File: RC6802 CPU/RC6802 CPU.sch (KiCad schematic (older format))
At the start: 53 parts, among them J1 RC6802_Backplane, J2 RC6802_UI_Port, J3 BARREL_JACK, J4 DECODED, M1 Mounting, M2 Mounting, M3 Mounting, M4 Mounting, U1 MC6802, U2 HM62256BLP-7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

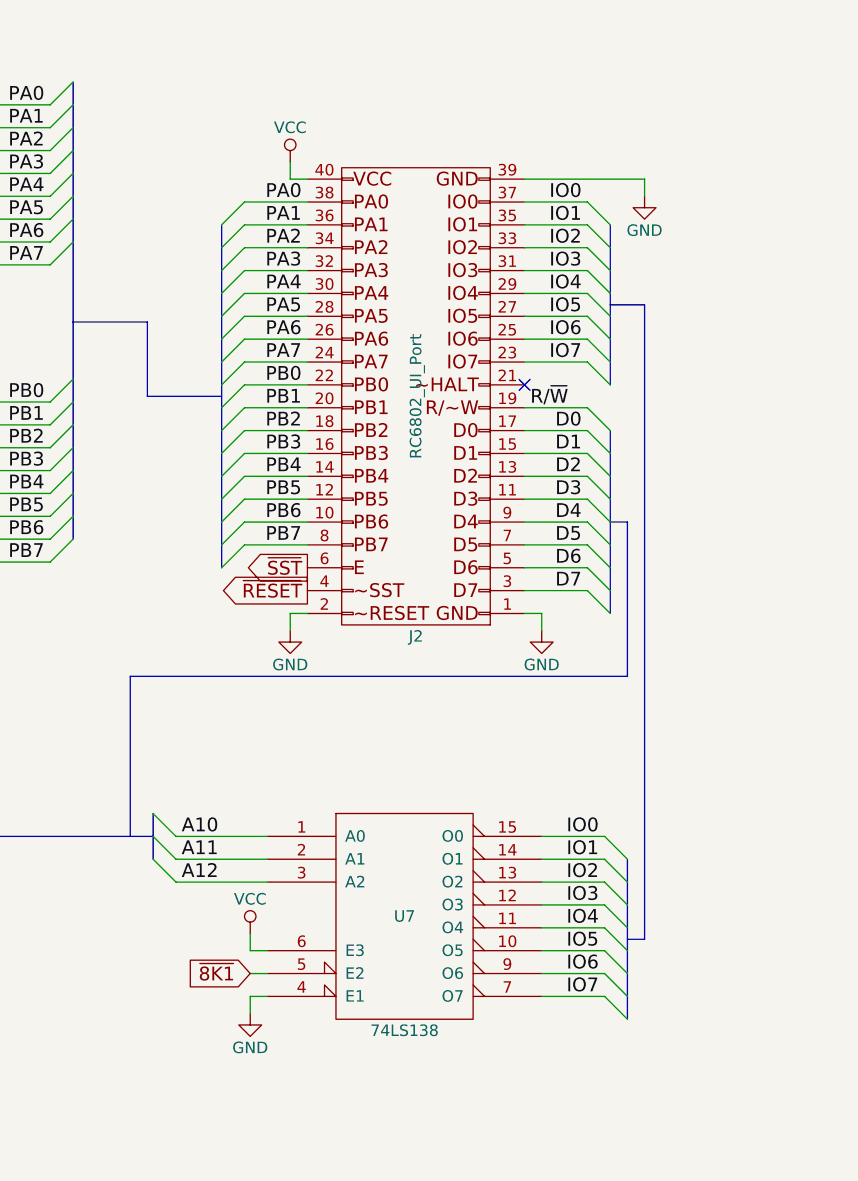
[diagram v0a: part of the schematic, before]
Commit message: UI board layout done
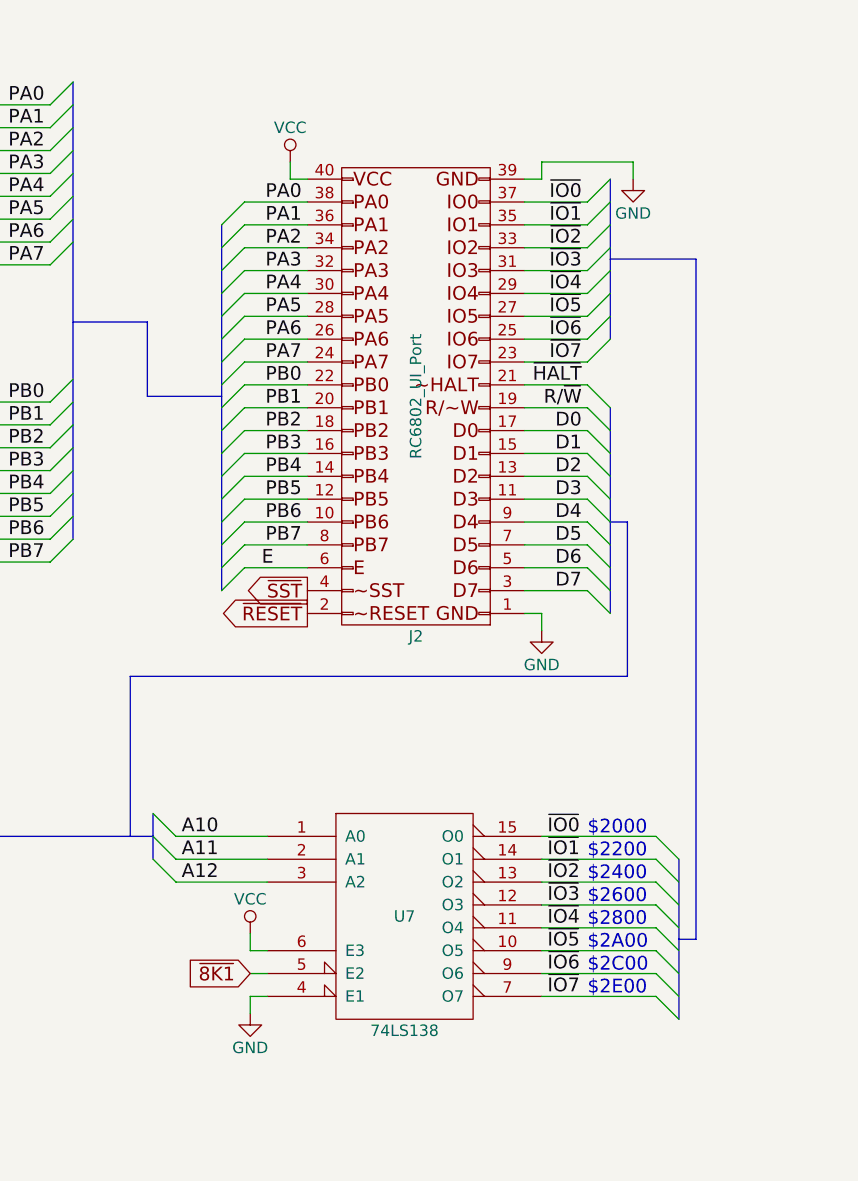
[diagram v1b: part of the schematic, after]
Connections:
- net E: now also J2.6 (P6)
- net GND: no longer J2.2 (P2)
- net ~HALT: now also J2.21 (P21)
- net ~RESET: now also J2.2 (P2); no longer J2.4 (P4)
- net ~SST: now also J2.4 (P4); no longer J2.6 (P6)
- net IO0 renamed ~IO0
- net IO1 renamed ~IO1
- net IO2 renamed ~IO2
- net IO3 renamed ~IO3
- net IO4 renamed ~IO4
- net IO5 renamed ~IO5
- net IO6 renamed ~IO6
- net IO7 renamed ~IO7
- no-connect marks 17 -> 16
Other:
- note added: "$2200"
- note added: "$2400"
- note added: "$2600"
- note added: "$2800"
- note added: "$2A00"
- note added: "$2C00"
- note added: "$2E00"
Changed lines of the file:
@@
 L GND #PWR05
 U 1 1 5D65DEF6
-P 10725 2425
-F 0 "#PWR05" H 10725 2175 50  0001 C CNN
-F 1 "GND" H 10725 2275 50  0000 C CNN
-F 2 "" H 10725 2425 50  0001 C CNN
-F 3 "" H 10725 2425 50  0001 C CNN
-	1    10725 2425
+P 10675 2350
+F 0 "#PWR05" H 10675 2100 50  0001 C CNN
+F 1 "GND" H 10675 2200 50  0000 C CNN
+F 2 "" H 10675 2350 50  0001 C CNN
+F 3 "" H 10675 2350 50  0001 C CNN
+	1    10675 2350
 	1    0    0    -1
 $EndComp
@@
 $EndComp
 $Comp
-L GND #PWR010
-U 1 1 5D729D92
-P 9175 4325
-F 0 "#PWR010" H 9175 4075 50  0001 C CNN
-F 1 "GND" H 9175 4175 50  0000 C CNN
-F 2 "" H 9175 4325 50  0001 C CNN
-F 3 "" H 9175 4325 50  0001 C CNN
-	1    9175 4325
-	1    0    0    -1
-$EndComp
-$Comp
 L GND #PWR011
 U 1 1 5D72A34D
@@
 	1    0    0    -1
 $EndComp
-Text Label 10525 5225 2    60   ~ 0
-IO0
-Text Label 10525 5325 2    60   ~ 0
-IO1
-Text Label 10525 5425 2    60   ~ 0
-IO2
-Text Label 10525 5525 2    60   ~ 0
-IO3
-Text Label 10525 5625 2    60   ~ 0
-IO4
-Text Label 10525 5725 2    60   ~ 0
-IO5
-Text Label 10525 5825 2    60   ~ 0
-IO6
-Text Label 10525 5925 2    60   ~ 0
-IO7
-Entry Wire Line
-	10650 5925 10550 5825
-Entry Wire Line
-	10650 5825 10550 5725
-Entry Wire Line
-	10650 5725 10550 5625
-Entry Wire Line
-	10650 5625 10550 5525
-Entry Wire Line
-	10650 5525 10550 5425
-Entry Wire Line
-	10650 5425 10550 5325
-Entry Wire Line
-	10650 5325 10550 5225
-Entry Wire Line
-	10650 6025 10550 5925
+Text Label 10300 5225 0    60   ~ 0
+~IO0
+Text Label 10300 5325 0    60   ~ 0
+~IO1
+Text Label 10300 5425 0    60   ~ 0
+~IO2
+Text Label 10300 5525 0    60   ~ 0
+~IO3
+Text Label 10300 5625 0    60   ~ 0
+~IO4
+Text Label 10300 5725 0    60   ~ 0
+~IO5
+Text Label 10300 5825 0    60   ~ 0
+~IO6
+Text Label 10300 5925 0    60   ~ 0
+~IO7
+Entry Wire Line
+	10875 5925 10775 5825
+Entry Wire Line
+	10875 5825 10775 5725
+Entry Wire Line
+	10875 5725 10775 5625
+Entry Wire Line
+	10875 5625 10775 5525
+Entry Wire Line
+	10875 5525 10775 5425
+Entry Wire Line
+	10875 5425 10775 5325
+Entry Wire Line
+	10875 5325 10775 5225
+Entry Wire Line
+	10875 6025 10775 5925
 Text Label 10450 2450 2    60   ~ 0
-IO0
+~IO0
 Text Label 10450 2550 2    60   ~ 0
-IO1
+~IO1
 Text Label 10450 2650 2    60   ~ 0
-IO2
+~IO2
 Text Label 10450 2750 2    60   ~ 0
-IO3
+~IO3
 Text Label 10450 2850 2    60   ~ 0
-IO4
+~IO4
 Text Label 10450 2950 2    60   ~ 0
-IO5
+~IO5
 Text Label 10450 3050 2    60   ~ 0
-IO6
+~IO6
 Text Label 10450 3150 2    60   ~ 0
-IO7
-Entry Wire Line
-	10575 3150 10475 3050
-Entry Wire Line
-	10575 3050 10475 2950
-Entry Wire Line
-	10575 2950 10475 2850
-Entry Wire Line
-	10575 2850 10475 2750
-Entry Wire Line
-	10575 2750 10475 2650
-Entry Wire Line
-	10575 2650 10475 2550
-Entry Wire Line
-	10575 2550 10475 2450
-Entry Wire Line
-	10575 3250 10475 3150
-Text Label 10225 3350 0    60   ~ 0
+~IO7
+Entry Wire Line
+	10575 2450 10475 2550
+Entry Wire Line
+	10575 2550 10475 2650
+Entry Wire Line
+	10575 2650 10475 2750
+Entry Wire Line
+	10575 2750 10475 2850
+Entry Wire Line
+	10575 2850 10475 2950
+Entry Wire Line
+	10575 2950 10475 3050
+Entry Wire Line
+	10575 3050 10475 3150
+Entry Wire Line
+	10575 2350 10475 2450
+Text Label 10450 3350 2    60   ~ 0
 R/~W
 Entry Wire Line
 	10575 3450 10475 3350
-NoConn ~ 10200 3250
 Wire Wire Line
 	15750 1150 15850 1150
@@
 	4950 4125 4550 4125
 Wire Wire Line
-	10200 2350 10725 2350
-Wire Wire Line
-	10725 2350 10725 2425
+	10275 2275 10675 2275
 Wire Wire Line
 	9175 2275 9175 2350
@@
 	8975 3750 9250 3750
 Wire Bus Line
-	8875 2550 8875 4050
-Wire Bus Line
-	10575 3450 10575 4250
+	8875 2550 8875 4150
+Wire Bus Line
+	10575 3350 10575 4250
 Wire Wire Line
 	15125 7550 14725 7550
@@
 	8575 5125 8575 5325
 Wire Wire Line
-	10275 5225 10550 5225
-Wire Wire Line
-	10275 5325 10550 5325
-Wire Wire Line
-	10275 5425 10550 5425
-Wire Wire Line
-	10275 5525 10550 5525
-Wire Wire Line
-	10275 5625 10550 5625
-Wire Wire Line
-	10275 5925 10550 5925
-Wire Wire Line
-	10275 5825 10550 5825
-Wire Wire Line
-	10275 5725 10550 5725
-Wire Bus Line
-	10650 5325 10650 6025
+	10275 5225 10775 5225
+Wire Wire Line
+	10275 5325 10775 5325
+Wire Wire Line
+	10275 5425 10775 5425
+Wire Wire Line
+	10275 5525 10775 5525
+Wire Wire Line
+	10275 5625 10775 5625
+Wire Wire Line
+	10275 5925 10775 5925
+Wire Wire Line
+	10275 5825 10775 5825
+Wire Wire Line
+	10275 5725 10775 5725
+Wire Bus Line
+	10875 5325 10875 6025
 Wire Wire Line
 	10200 2450 10475 2450
@@
 	10200 3350 10475 3350
 Wire Bus Line
-	10575 2550 10575 3250
-Wire Bus Line
-	10575 2900 10725 2900
+	10575 2350 10575 3050
 Wire Bus Line
 	8550 2975 8550 3300
@@
 	8550 3300 8875 3300
 Wire Bus Line
-	10650 5675 10725 5675
-Wire Bus Line
-	10725 5675 10725 2900
+	10950 5675 10875 5675
+Wire Bus Line
+	10950 2700 10950 5675
 Wire Bus Line
 	8575 5225 5475 5225
@@
 	11325 7850 11725 7850
 Connection ~ 11725 7850
+Text GLabel 9250 4250 0    60   Output ~ 0
+~RESET
 Text GLabel 9250 4150 0    60   Output ~ 0
-~RESET
-Text GLabel 9250 4050 0    60   Output ~ 0
 ~SST
-Wire Wire Line
-	9250 4250 9175 4250
-Wire Wire Line
-	9175 4250 9175 4325
 Wire Wire Line
 	10200 4250 10275 4250
@@
 Text Notes 11825 10350 0    60   ~ 0
 RC6802 Microchicken computer as explained in the book "22 Micro-computer projects:\nTo build, use and learn" by Daniel Metzger. Hardware changed slightly to add a\nsecondary 74LS138 to further divide device area ($2000-$3FFF), original addresses used\nin code examples should be unchanged from original memory map.
+Text Label 9050 4050 0    60   ~ 0
+E
+Wire Wire Line
+	9250 4050 8975 4050
+Entry Wire Line
+	8975 4050 8875 4150
+Text Label 10450 3250 2    60   ~ 0
+~HALT
+Wire Wire Line
+	10200 3250 10475 3250
+Entry Wire Line
+	10575 3350 10475 3250
+Wire Bus Line
+	10575 2700 10950 2700
+Wire Wire Line
+	10200 2350 10275 2350
+Wire Wire Line
+	10275 2350 10275 2275
+Wire Wire Line
+	10675 2275 10675 2350
+Text Notes 10475 5225 0    60   ~ 0
+$2000
+Text Notes 10475 5325 0    60   ~ 0
+$2200
+Text Notes 10475 5425 0    60   ~ 0
+$2400
+Text Notes 10475 5525 0    60   ~ 0
+$2600
+Text Notes 10475 5625 0    60   ~ 0
+$2800
+Text Notes 10475 5725 0    60   ~ 0
+$2A00
+Text Notes 10475 5825 0    60   ~ 0
+$2C00
+Text Notes 10475 5925 0    60   ~ 0
+$2E00
 $EndSCHEMATC

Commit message: Added /VMA to backplane
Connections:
- net E: now also U5.6 (E3); no longer U4.1
- net VMA: now also U4.1; no longer J1.26 (SYNC), U5.6 (E3)
- net ~8K1: now also J1.21 (PHI0)
- net ~VMA: now reaches U4.2, U5.5 (E2)
- net ~VMA: now also J1.26 (SYNC)
- no-connect marks 16 -> 15
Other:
- moved on the sheet: U4A, U7

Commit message: Added VMA_E signal to backplane
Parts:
- removed U4: 74LS04, Housings_DIP:DIP-14_W7.62mm_Socket, symbol 74LS04
- added U4: 74LS00, Housings_DIP:DIP-14_W7.62mm_Socket, symbol 74LS00
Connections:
- net 8K4 is gone; now on net ~8K4: J4.2 (Pin_2)
- net 8K5 is gone; now on net ~8K5: J4.3 (Pin_3)
- net E: now also J1.21 (PHI0), U4.1; no longer J1.19 (PHI2), U5.6 (E3)
- net GND: now also U5.5 (E2), U4.10, U4.12, U4.13, U4.7 (GND), U4.7 (GND), U4.7 (GND), U4.7 (GND), U4.9
- net VCC: now also U4.14 (VCC), U4.14 (VCC), U4.14 (VCC), U4.14 (VCC)
- net VMA: now also J1.26 (SYNC), U4.2
- net ~8K1: now also J1.39 (P39); no longer J1.21 (PHI0)
- removed net ~VMA: J1.26 (SYNC), U5.5 (E2)
- new net: U4.3, U4.4, U4.5
- new net VMA_E: J1.19 (PHI2), U4.6, U5.6 (E3)
- no-connect marks 15 -> 13
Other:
- moved on the sheet: JP2, U5

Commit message: Updated software
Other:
- note added: "A"
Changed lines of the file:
@@
 Text Label 3800 7125 0    60   ~ 0
 ~8K5
+Text Notes 15400 11075 0    60   ~ 0
+A
 $EndSCHEMATC

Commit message: Fixed CPU bugs
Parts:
- C11, C9: value 33pF -> 22pF

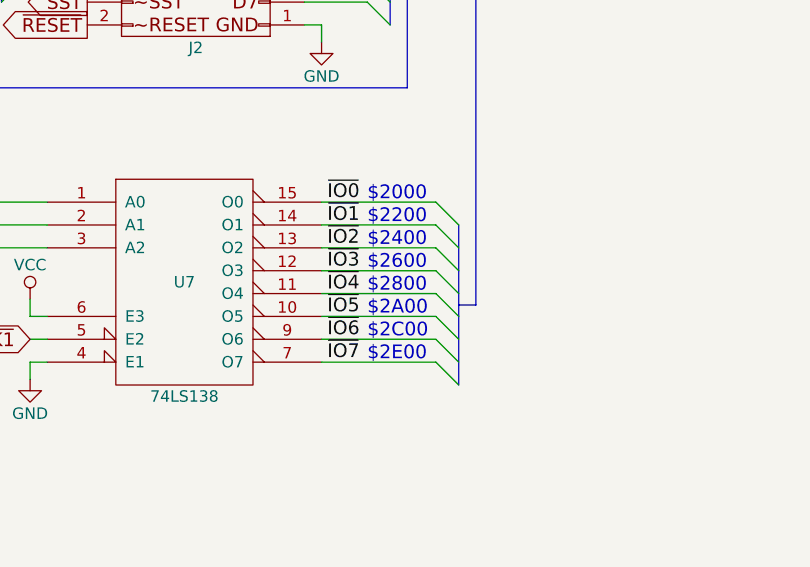
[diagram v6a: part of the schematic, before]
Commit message: Schematic had wrong I/O addresses
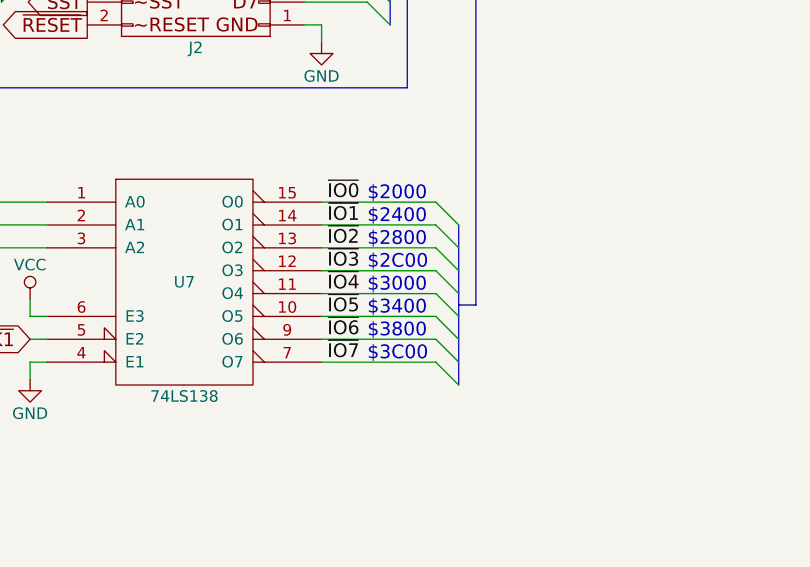
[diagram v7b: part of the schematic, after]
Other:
- note added: "$3000"
- note added: "$3400"
- note added: "$3800"
- note added: "$3C00"
- note removed: "$2200"
- note removed: "$2600"
- note removed: "$2A00"
- note removed: "$2E00"
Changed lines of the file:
@@
 $2000
 Text Notes 10475 5125 0    60   ~ 0
-$2200
+$2400
 Text Notes 10475 5225 0    60   ~ 0
-$2400
+$2800
 Text Notes 10475 5325 0    60   ~ 0
-$2600
+$2C00
 Text Notes 10475 5425 0    60   ~ 0
-$2800
+$3000
 Text Notes 10475 5525 0    60   ~ 0
-$2A00
+$3400
 Text Notes 10475 5625 0    60   ~ 0
-$2C00
+$3800
 Text Notes 10475 5725 0    60   ~ 0
-$2E00
+$3C00
 Text GLabel 15050 5950 0    60   Input ~ 0
 ~8K1
